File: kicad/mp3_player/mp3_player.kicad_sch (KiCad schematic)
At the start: 24 parts, among them J1 microSD, SW1 Boot, SW2 Reset, SW3 RotaryEncoder_Switch, U1 MPU6500-breakout, U2 HC-SR04_Ultrasonic_Sensor, U3 ESP32-S3-WROOM-1, U4 AHT20_BMP280

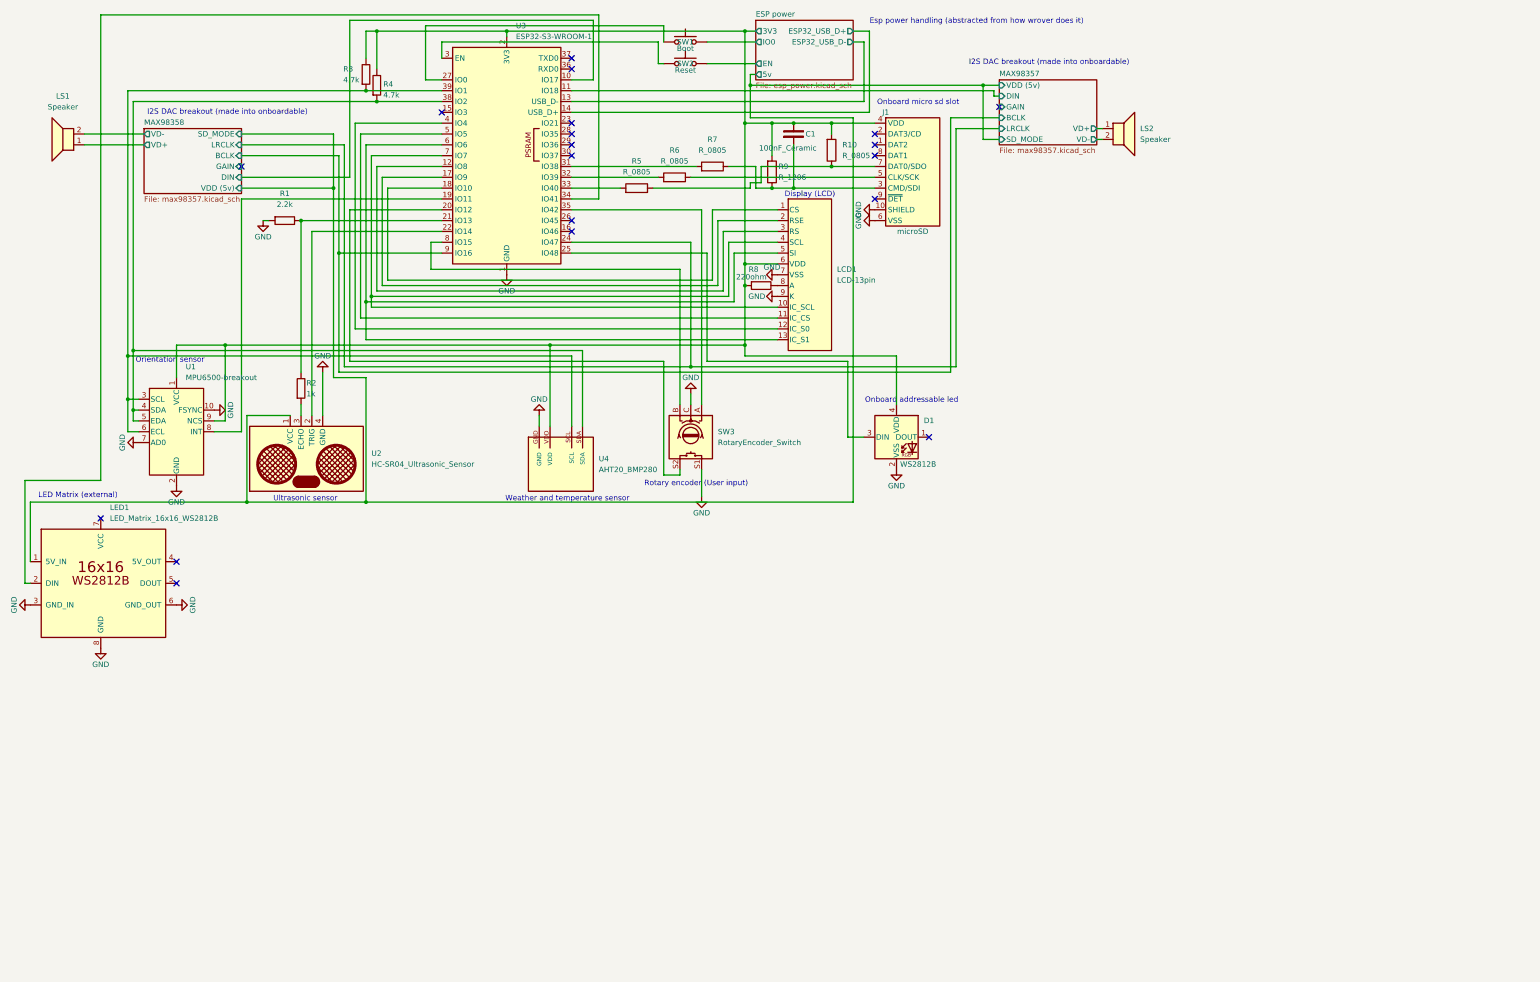
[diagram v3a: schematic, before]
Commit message: [ADD] lcd segment displays to the project
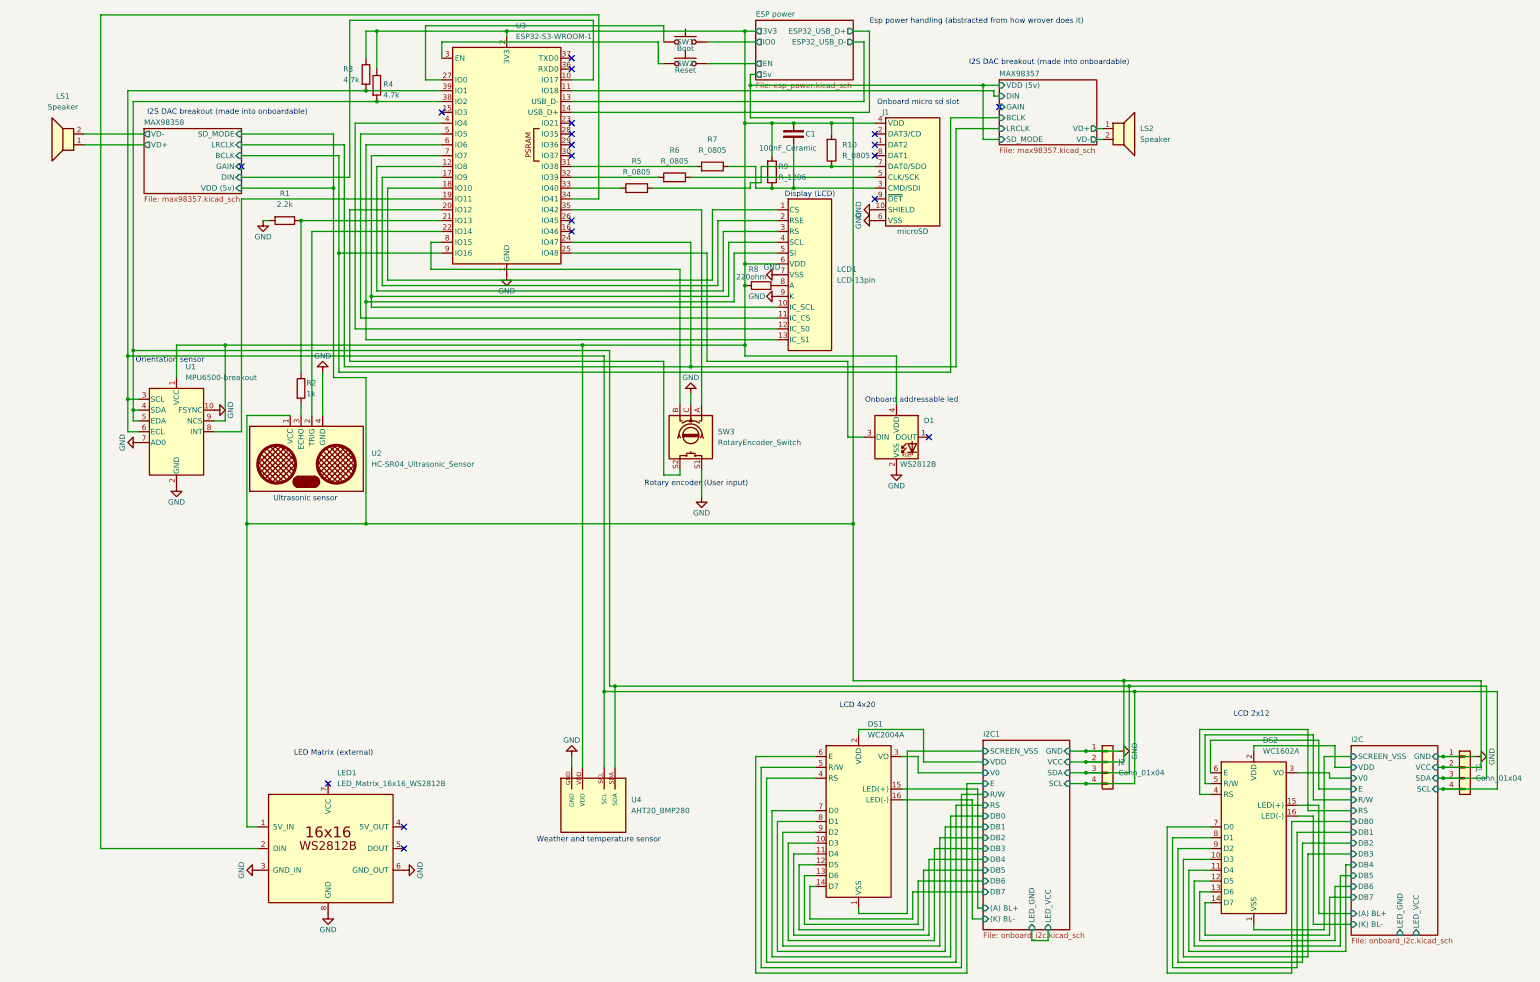
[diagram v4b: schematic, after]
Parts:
- added DS1: WC2004A, Display:WC1602A, symbol Display_Character:WC1602A
- added DS2: WC1602A, Display:WC1602A, symbol Display_Character:WC1602A
- added J2, J3: Conn_01x04, PCM_4ms_Connector:Pins_1x04_3.96mm_TH_MTA156, symbol PCM_4ms_Connector:Conn_01x04
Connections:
- net ESP power/5v: now also J2.2 (Pin_2), J3.2 (Pin_2)
- net GND: now also J2.1 (Pin_1), J3.1 (Pin_1)
- net I2C/SDA: now reaches R4.1, U1.4 (SDA), U1.5 (EDA), U3.38 (IO2), U4.SDA
- net I2C/SDA: now also J2.3 (Pin_3), J3.3 (Pin_3)
- net I2C/SCL: now reaches R3.1, U1.3 (SCL), U1.6 (ECL), U3.39 (IO1), U4.SCL
- net I2C/SCL: now also J2.4 (Pin_4), J3.4 (Pin_4)
- new net I2C/(A) BL+: DS2.15 (LED(+))
- new net I2C/(K) BL-: DS2.16 (LED(-))
- new net I2C/DB0: DS2.7 (D0)
- new net I2C/DB1: DS2.8 (D1)
- new net I2C/DB2: DS2.9 (D2)
- new net I2C/DB3: DS2.10 (D3)
- new net I2C/DB4: DS2.11 (D4)
- new net I2C/DB5: DS2.12 (D5)
- new net I2C/DB6: DS2.13 (D6)
- new net I2C/DB7: DS2.14 (D7)
- new net I2C/E: DS2.6 (E)
- new net I2C/RS: DS2.4 (RS)
- new net I2C/R/W: DS2.5 (R/W)
- new net I2C/SCREEN_VSS: DS2.1 (VSS)
- new net I2C/V0: DS2.3 (VO)
- new net I2C/VDD: DS2.2 (VDD)
- new net I2C1/(A) BL+: DS1.15 (LED(+))
- new net I2C1/(K) BL-: DS1.16 (LED(-))
- new net I2C1/DB0: DS1.7 (D0)
- new net I2C1/DB1: DS1.8 (D1)
- new net I2C1/DB2: DS1.9 (D2)
- new net I2C1/DB3: DS1.10 (D3)
- new net I2C1/DB4: DS1.11 (D4)
- new net I2C1/DB5: DS1.12 (D5)
- new net I2C1/DB6: DS1.13 (D6)
- new net I2C1/DB7: DS1.14 (D7)
- new net I2C1/E: DS1.6 (E)
- new net I2C1/RS: DS1.4 (RS)
- new net I2C1/R/W: DS1.5 (R/W)
- new net I2C1/SCREEN_VSS: DS1.1 (VSS)
- new net I2C1/V0: DS1.3 (VO)
- new net I2C1/VDD: DS1.2 (VDD)
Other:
- added sheet I2C (onboard_i2c.kicad_sch)
- added sheet I2C1 (onboard_i2c.kicad_sch)
- note added: "LCD 2x12"
- note added: "LCD 4x20"
- title: (none) -> The bloated mp3 player.
- moved on the sheet: LED1, U4

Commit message: [UPDATE] the KiCad schematic to show the pins requiring bridging on the I2C
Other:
- sheet I2C ports: added A0(1), A0(2), A1(1), A1(2), A2(1), A2(2); removed none
- sheet I2C1 ports: added A0(1), A0(2), A1(1), A1(2), A2(1), A2(2); removed none
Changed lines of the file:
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@@
 	(wire
 		(pts
+			(xy 265.43 196.85) (xy 267.97 196.85)
+		)
+		(stroke
+			(width 0)
+			(type default)
+		)
+	)
+	(wire
+		(pts
 			(xy 44.45 102.87) (xy 44.45 110.49)
 		)
@@
 	(wire
 		(pts
+			(xy 265.43 199.39) (xy 267.97 199.39)
+		)
+		(stroke
+			(width 0)
+			(type default)
+		)
+	)
+	(wire
+		(pts
 			(xy 100.33 88.9) (xy 196.85 88.9)
 		)
@@
 	(wire
 		(pts
+			(xy 267.97 196.85) (xy 267.97 199.39)
+		)
+		(stroke
+			(width 0)
+			(type default)
+		)
+	)
+	(wire
+		(pts
 			(xy 231.14 187.96) (xy 245.11 187.96)
 		)
@@
 			)
 		)
+		(pin "A0(1)" input
+			(at 351.79 199.39 0)
+			(effects
+				(font
+					(size 1.27 1.27)
+				)
+				(justify right)
+			)
+		)
+		(pin "A0(2)" input
+			(at 351.79 201.93 0)
+			(effects
+				(font
+					(size 1.27 1.27)
+				)
+				(justify right)
+			)
+		)
+		(pin "A1(1)" input
+			(at 351.79 205.74 0)
+			(effects
+				(font
+					(size 1.27 1.27)
+				)
+				(justify right)
+			)
+		)
+		(pin "A1(2)" input
+			(at 351.79 208.28 0)
+			(effects
+				(font
+					(size 1.27 1.27)
+				)
+				(justify right)
+			)
+		)
+		(pin "A2(1)" input
+			(at 351.79 213.36 0)
+			(effects
+				(font
+					(size 1.27 1.27)
+				)
+				(justify right)
+			)
+		)
+		(pin "A2(2)" input
+			(at 351.79 215.9 0)
+			(effects
+				(font
+					(size 1.27 1.27)
+				)
+				(justify right)
+			)
+		)
 		(instances
 			(project "mp3_player"
@@
 			)
 		)
+		(pin "A0(1)" input
+			(at 265.43 196.85 0)
+			(effects
+				(font
+					(size 1.27 1.27)
+				)
+				(justify right)
+			)
+		)
+		(pin "A0(2)" input
+			(at 265.43 199.39 0)
+			(effects
+				(font
+					(size 1.27 1.27)
+				)
+				(justify right)
+			)
+		)
+		(pin "A1(1)" input
+			(at 265.43 203.2 0)
+			(effects
+				(font
+					(size 1.27 1.27)
+				)
+				(justify right)
+			)
+		)
+		(pin "A1(2)" input
+			(at 265.43 205.74 0)
+			(effects
+				(font
+					(size 1.27 1.27)
+				)
+				(justify right)
+			)
+		)
+		(pin "A2(1)" input
+			(at 265.43 209.55 0)
+			(effects
+				(font
+					(size 1.27 1.27)
+				)
+				(justify right)
+			)
+		)
+		(pin "A2(2)" input
+			(at 265.43 212.09 0)
+			(effects
+				(font
+					(size 1.27 1.27)
+				)
+				(justify right)
+			)
+		)

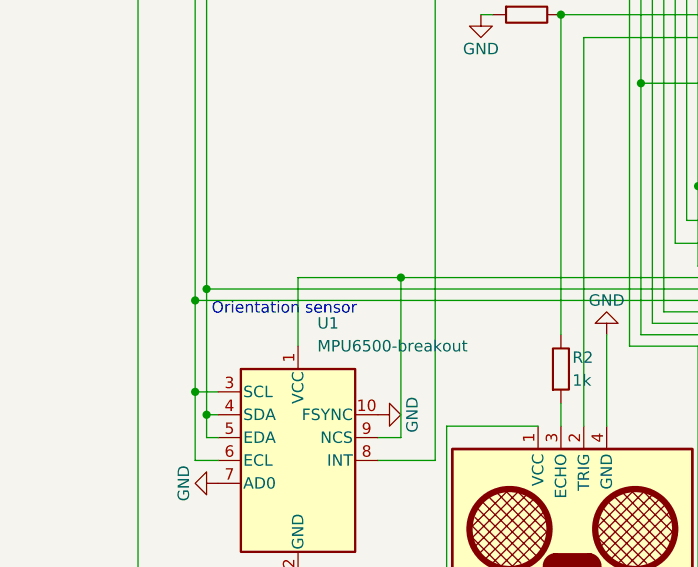
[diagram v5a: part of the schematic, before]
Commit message: [UPDATE] the schematic to include the power help to avoid a crash or lcd corruption due to brown outs
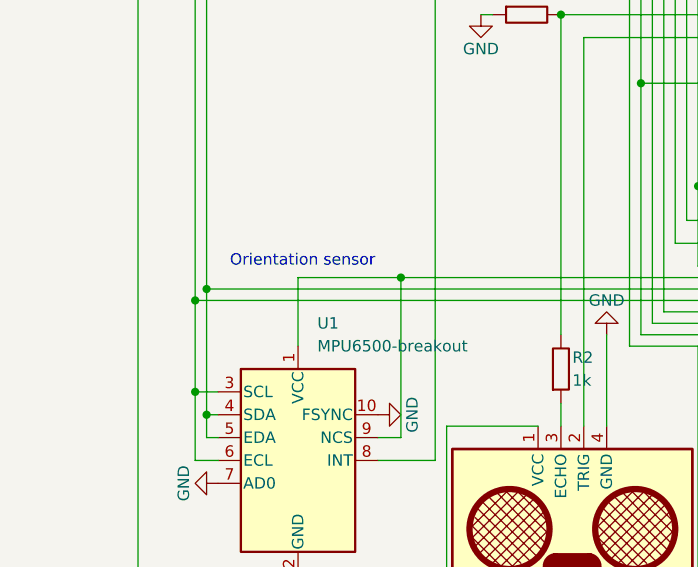
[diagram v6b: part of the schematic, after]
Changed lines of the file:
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@@
 	(text "Orientation sensor"
 		(exclude_from_sim no)
-		(at 54.356 93.726 0)
+		(at 56.388 88.392 0)
 		(effects
 			(font
